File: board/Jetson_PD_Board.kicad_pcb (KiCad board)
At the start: 2 copper layers, 28 parts, among them J1 USB4081-03-A, J2 768250002, Q1 NTTFS5C673NLTAG, Q2 NTTFS5C673NLTAG, Q3 NTTFS5C673NLTAG, U1 APK43070DKZ-13-FA01, U2 USBLC6-2SC6

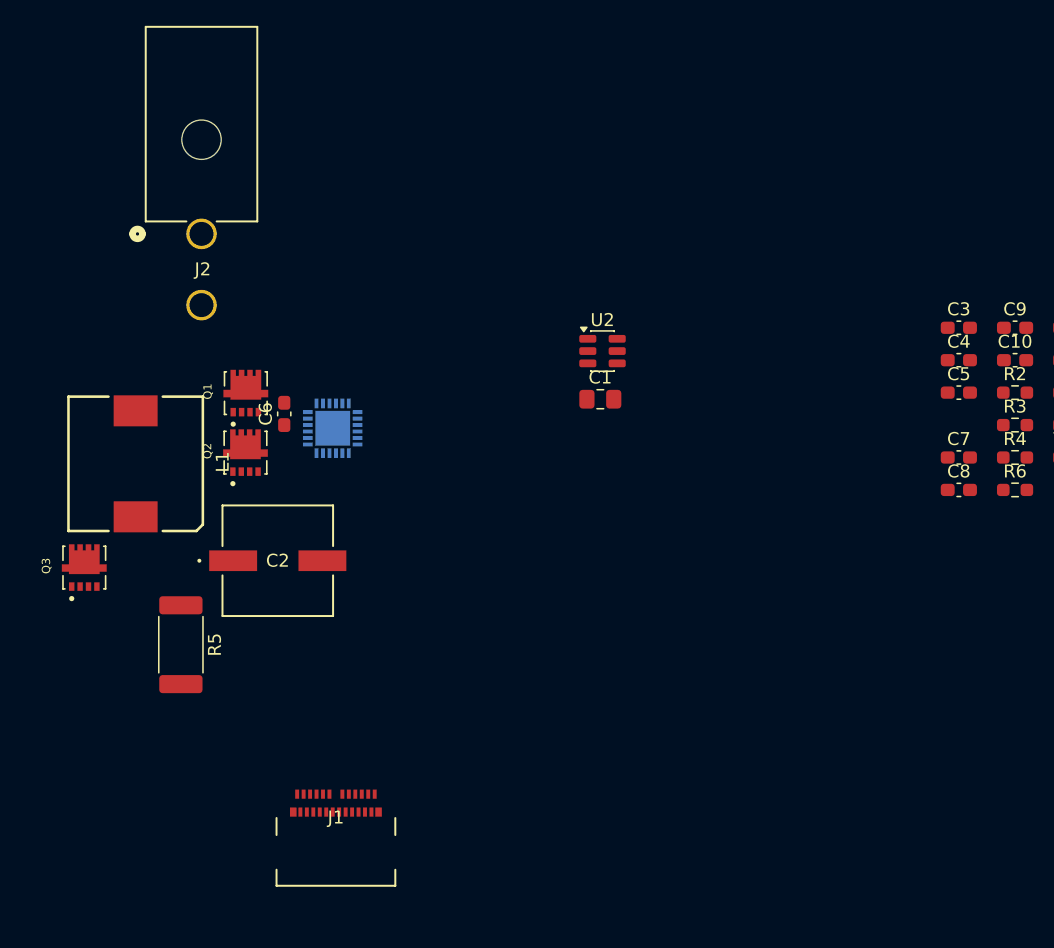
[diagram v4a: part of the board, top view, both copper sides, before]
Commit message: Labeled switching node
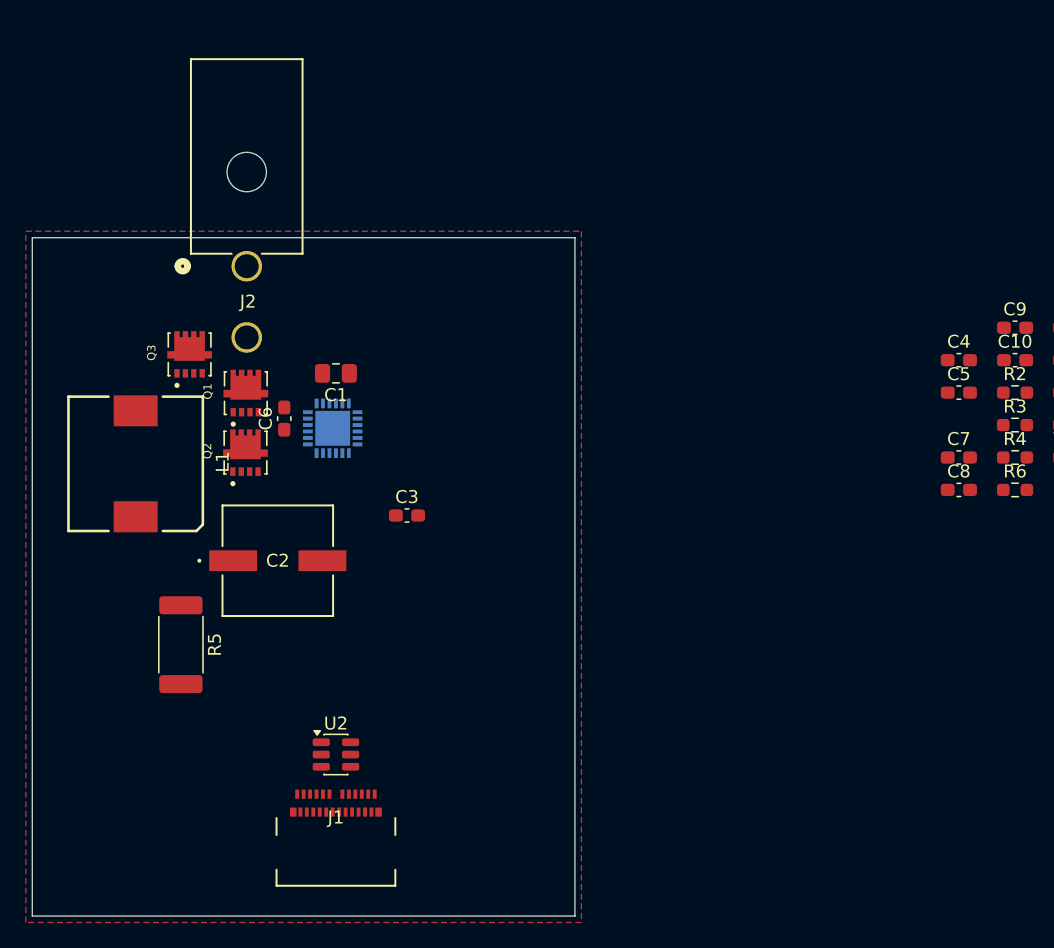
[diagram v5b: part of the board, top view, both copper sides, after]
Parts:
- moved C3 45.1 mm to (147.5, 105.5)
- moved U2 37.4 mm to (142.0, 124.0)
- moved C1 20.6 mm to (142.0, 94.5), turned to 180 degrees
- moved Q3 18.4 mm to (130.7, 93.0)
- moved J2 4.30 mm to (135.1, 86.2)
- moved C6 0.36 mm to (138.0, 98.0)
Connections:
- net Net-(Q1-S) renamed /Switching_Node
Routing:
- added copper zone on F.Cu, net GND
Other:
- board outline added: 42 x 52.5 mm
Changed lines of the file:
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@@
 	(net 6 "Net-(C5-Pad1)")
 	(net 7 "Net-(U1-VFB)")
-	(net 8 "Net-(Q1-S)")
+	(net 8 "/Switching_Node")
 	(net 9 "Net-(U1-BST)")
 	(net 10 "Net-(U1-V5V)")
@@
 			(size 2.4 3.4)
 			(layers "F.Cu" "F.Mask" "F.Paste")
-			(net 8 "Net-(Q1-S)")
+			(net 8 "/Switching_Node")
 			(pinfunction "1")
 			(pintype "passive")
@@
 	(footprint "PD_Hardware_Footprints:TRANS_NVTFS5116PLTAG"
 		(layer "F.Cu")
-		(at 122.525 109.53 90)
+		(at 130.675 93.03 90)
 		(property "Reference" "Q3"
 			(at 0.127 -2.9464 90)
@@
 			(size 0.66 0.42)
 			(layers "F.Cu" "F.Mask")
-			(net 8 "Net-(Q1-S)")
+			(net 8 "/Switching_Node")
 			(pinfunction "S")
 			(pintype "passive")
@@
 			(size 0.66 0.42)
 			(layers "F.Cu" "F.Mask")
-			(net 8 "Net-(Q1-S)")
+			(net 8 "/Switching_Node")
 			(pinfunction "S")
 			(pintype "passive")
@@
 			(size 0.66 0.42)
 			(layers "F.Cu" "F.Mask")
-			(net 8 "Net-(Q1-S)")
+			(net 8 "/Switching_Node")
 			(pinfunction "S")
 			(pintype "passive")
@@
 	(footprint "Package_TO_SOT_SMD:SOT-23-6"
 		(layer "F.Cu")
-		(at 162.6325 92.775)
+		(at 142 124)
 		(descr "SOT, 6 Pin (JEDEC MO-178 Var AB https://www.jedec.org/document_search?search_api_views_fulltext=MO-178), generated with kicad-footprint-generator ipc_gullwing_generator.py")
 		(tags "SOT TO_SOT_SMD")
@@
 	(footprint "PD_Hardware_Footprints:CONN_SD-76825-0100_02_MOL"
 		(layer "F.Cu")
-		(at 131.5969 83.70535 180)
+		(at 135.0969 86.20535 180)
 		(property "Reference" "J2"
 			(at -0.1016 -2.7432 0)
@@
 	(footprint "Capacitor_SMD:C_0805_2012Metric_Pad1.18x1.45mm_HandSolder"
 		(layer "F.Cu")
-		(at 162.4625 96.5)
+		(at 142 94.5 180)
 		(descr "Capacitor SMD 0805 (2012 Metric), square (rectangular) end terminal, IPC-7351 nominal with elongated pad for handsoldering. (Body size source: IPC-SM-782 page 76, https://www.pcb-3d.com/wordpress/wp-content/uploads/ipc-sm-782a_amendment_1_and_2.pdf, https://docs.google.com/spreadsheets/d/1BsfQQcO9C6DZCsRaXUlFlo91Tg2WpOkGARC1WS5S8t0/edit?usp=sharing), generated with kicad-footprint-generator")
 		(tags "capacitor handsolder")
@@
 		(attr smd)
 		(fp_line
-			(start -0.261252 -0.735)
-			(end 0.261252 -0.735)
+			(start -0.261252 0.735)
+			(end 0.261252 0.735)
 			(stroke
 				(width 0.12)
@@
 		)
 		(fp_line
-			(start -0.261252 0.735)
-			(end 0.261252 0.735)
+			(start -0.261252 -0.735)
+			(end 0.261252 -0.735)
 			(stroke
 				(width 0.12)
@@
 		)
 		(fp_line
-			(start -1.88 -0.98)
-			(end 1.88 -0.98)
+			(start 1.88 0.98)
+			(end -1.88 0.98)
 			(stroke
 				(width 0.05)
@@
 		)
 		(fp_line
-			(start -1.88 0.98)
-			(end -1.88 -0.98)
+			(start 1.88 -0.98)
+			(end 1.88 0.98)
 			(stroke
 				(width 0.05)
@@
 		)
 		(fp_line
-			(start 1.88 -0.98)
-			(end 1.88 0.98)
+			(start -1.88 0.98)
+			(end -1.88 -0.98)
 			(stroke
 				(width 0.05)
@@
 		)
 		(fp_line
-			(start 1.88 0.98)
-			(end -1.88 0.98)
+			(start -1.88 -0.98)
+			(end 1.88 -0.98)
 			(stroke
 				(width 0.05)
@@
 		)
 		(fp_line
-			(start -1 -0.625)
-			(end 1 -0.625)
+			(start 1 0.625)
+			(end -1 0.625)
 			(stroke
 				(width 0.1)
@@
 		)
 		(fp_line
-			(start -1 0.625)
-			(end -1 -0.625)
+			(start 1 -0.625)
+			(end 1 0.625)
 			(stroke
 				(width 0.1)
@@
 		)
 		(fp_line
-			(start 1 -0.625)
-			(end 1 0.625)
+			(start -1 0.625)
+			(end -1 -0.625)
 			(stroke
 				(width 0.1)
@@
 		)
 		(fp_line
-			(start 1 0.625)
-			(end -1 0.625)
+			(start -1 -0.625)
+			(end 1 -0.625)
 			(stroke
 				(width 0.1)
@@
 		)
 		(pad "1" smd roundrect
-			(at -1.0375 0)
+			(at -1.0375 0 180)
 			(size 1.175 1.45)
 			(layers "F.Cu" "F.Mask" "F.Paste")
@@
 		)
 		(pad "2" smd roundrect
-			(at 1.0375 0)
+			(at 1.0375 0 180)
 			(size 1.175 1.45)
 			(layers "F.Cu" "F.Mask" "F.Paste")
@@
 	(footprint "Capacitor_SMD:C_0603_1608Metric_Pad1.08x0.95mm_HandSolder"
 		(layer "F.Cu")
-		(at 190.2125 90.97)
+		(at 147.5 105.5)
 		(descr "Capacitor SMD 0603 (1608 Metric), square (rectangular) end terminal, IPC-7351 nominal with elongated pad for handsoldering. (Body size source: IPC-SM-782 page 76, https://www.pcb-3d.com/wordpress/wp-content/uploads/ipc-sm-782a_amendment_1_and_2.pdf), generated with kicad-footprint-generator")
 		(tags "capacitor handsolder")
@@
 	(footprint "Capacitor_SMD:C_0603_1608Metric_Pad1.08x0.95mm_HandSolder"
 		(layer "F.Cu")
-		(at 138 97.6375 90)
+		(at 138 98 90)
 		(descr "Capacitor SMD 0603 (1608 Metric), square (rectangular) end terminal, IPC-7351 nominal with elongated pad for handsoldering. (Body size source: IPC-SM-782 page 76, https://www.pcb-3d.com/wordpress/wp-content/uploads/ipc-sm-782a_amendment_1_and_2.pdf), generated with kicad-footprint-generator")
 		(tags "capacitor handsolder")
@@
 			(layers "F.Cu" "F.Mask" "F.Paste")
 			(roundrect_rratio 0.25)
-			(net 8 "Net-(Q1-S)")
+			(net 8 "/Switching_Node")
 			(pintype "passive")
 		)
@@
 			(size 0.635 1.27)
 			(layers "F.Cu")
-			(net 8 "Net-(Q1-S)")
+			(net 8 "/Switching_Node")
 			(pinfunction "D")
 			(pintype "passive")
@@
 			(size 0.75 0.3)
 			(layers "B.Cu" "B.Mask" "B.Paste")
-			(net 8 "Net-(Q1-S)")
+			(net 8 "/Switching_Node")
 			(pinfunction "SW")
 			(pintype "output")
@@
 			)
 		)
+	)
+	(gr_rect
+		(start 118.5 84)
+		(end 160.5 136.5)
+		(stroke
+			(width 0.05)
+			(type default)
+		)
+		(fill no)
+		(layer "Edge.Cuts")
+	)
+	(zone
+		(net 1)
+		(net_name "GND")
+		(layer "F.Cu")
+		(hatch edge 0.5)
+		(connect_pads
+			(clearance 0.5)
+		)
+		(min_thickness 0.25)
+		(filled_areas_thickness no)
+		(fill yes
+			(thermal_gap 0.5)
+			(thermal_bridge_width 0.5)
+		)
+		(polygon
+			(pts
+				(xy 118 83.5) (xy 161 83.5) (xy 161 137) (xy 118 137)
+			)
+		)

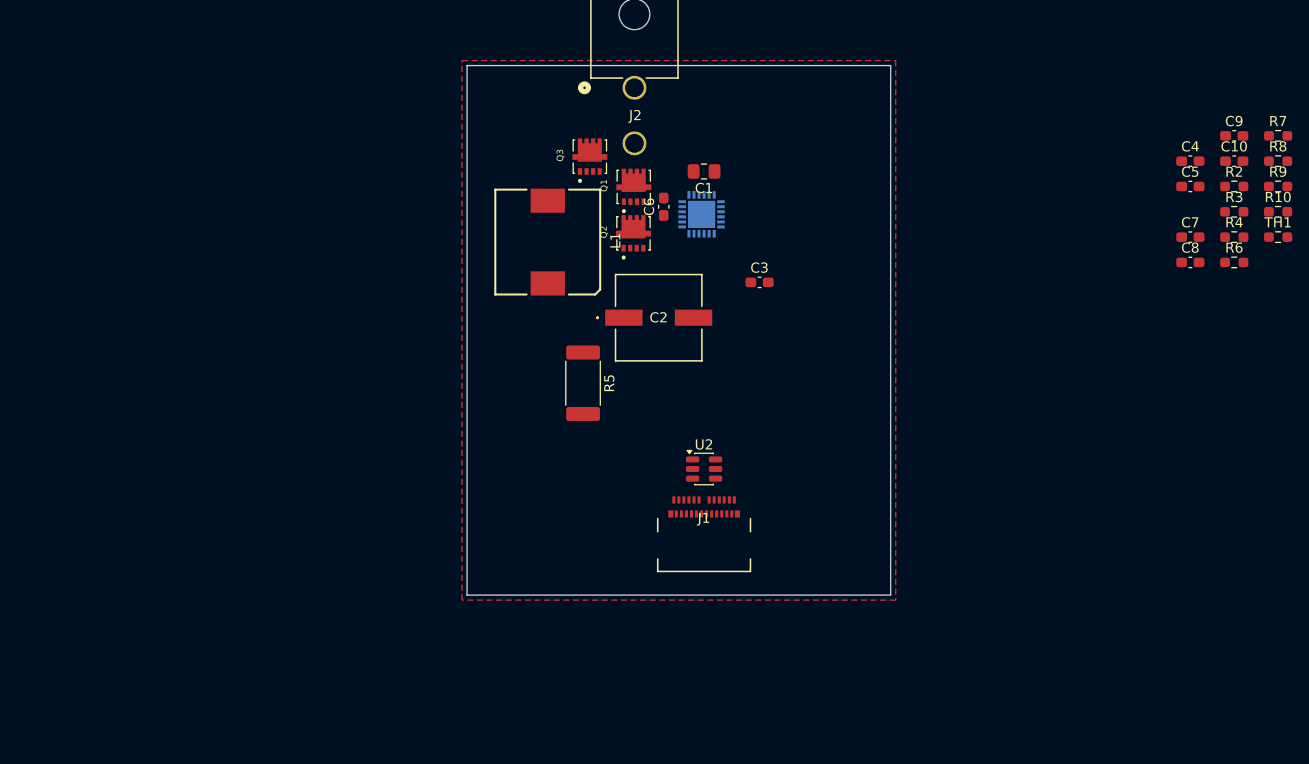
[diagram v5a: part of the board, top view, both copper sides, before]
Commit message: Added mounting holes, indicator LED, and cleaned up shcematic
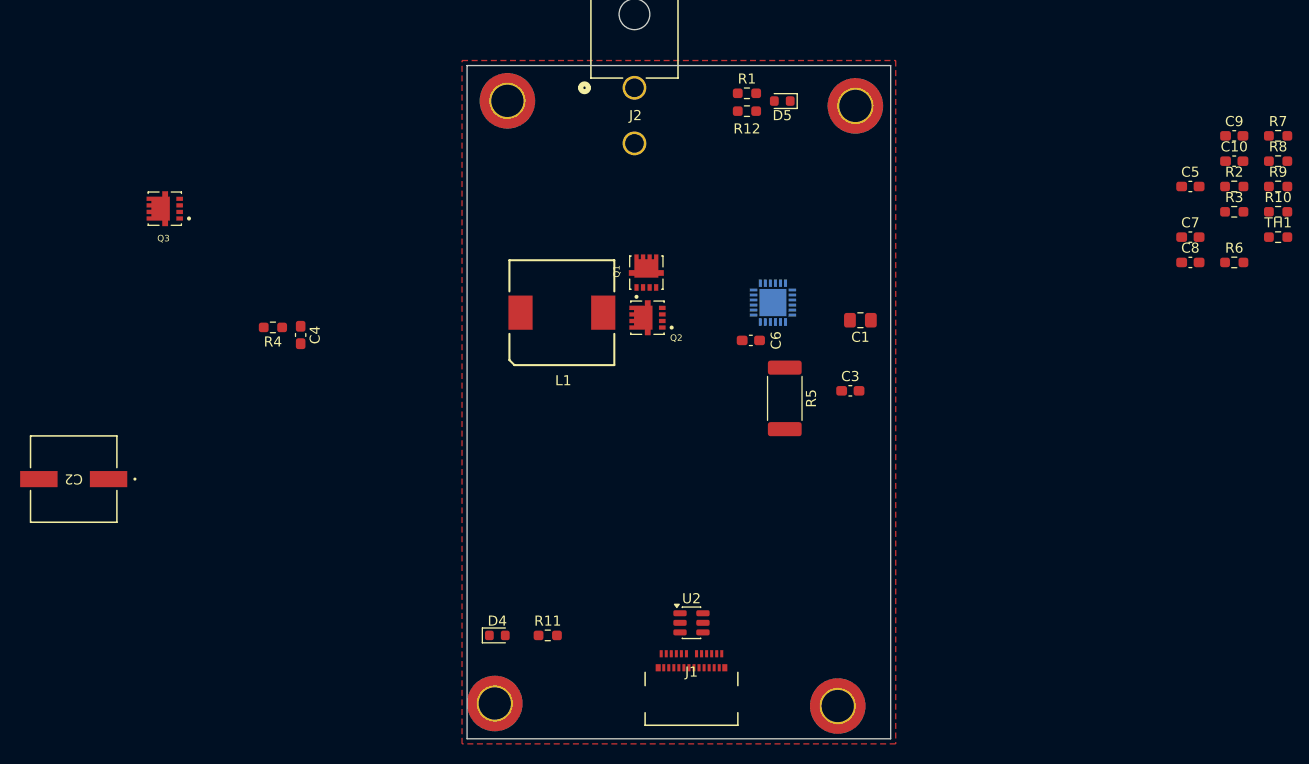
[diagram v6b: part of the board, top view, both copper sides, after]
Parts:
- added D4: LED (Blue), LED_SMD:LED_0603_1608Metric, F.Cu at (121.5, 140.5)
- added D5: LED (Yellow), LED_SMD:LED_0603_1608Metric, F.Cu at (149.8, 87.5)
- added H1: MountingHole, MountingHole:MountingHole_3.2mm_M3_ISO14580_Pad_TopBottom, F.Cu at (157.0, 88.0)
- added H2: MountingHole, MountingHole:MountingHole_3.2mm_M3_ISO14580_Pad_TopBottom, F.Cu at (121.2, 147.2)
- added H3: MountingHole, MountingHole:MountingHole_3.2mm_M3_ISO14580_Pad_TopBottom, F.Cu at (122.5, 87.5)
- added H4: MountingHole, MountingHole:MountingHole_3.2mm_M3_ISO14580_Pad_TopBottom, F.Cu at (155.2, 147.5)
- added R1: 2.2k, Resistor_SMD:R_0603_1608Metric_Pad0.98x0.95mm_HandSolder, F.Cu at (146.2, 86.8)
- added R11: 820, Resistor_SMD:R_0603_1608Metric_Pad0.98x0.95mm_HandSolder, F.Cu at (126.5, 140.5)
- added R12: 2.2k, Resistor_SMD:R_0603_1608Metric_Pad0.98x0.95mm_HandSolder, F.Cu at (146.2, 88.5)
- moved R4 95.7 mm to (99.2, 110.0), turned to 180 degrees
- moved C4 89.9 mm to (102.0, 110.7), turned to -90 degrees
- moved C2 60.2 mm to (79.5, 125.0), turned to 180 degrees
- moved Q3 42.5 mm to (88.5, 98.2), turned to 180 degrees
- moved C1 21.4 mm to (157.5, 109.2)
- moved R5 20.1 mm to (150.0, 117.0)
- moved C6 15.8 mm to (146.6, 111.2), turned to 0 degrees
- moved J1 15.3 mm to (140.8, 145.8)
- moved U2 15.3 mm to (140.8, 139.2)
- moved C3 14.0 mm to (156.5, 116.2)
- moved U1 11.3 mm to (148.8, 107.5)
- moved Q1 8.59 mm to (136.3, 104.5)
- moved Q2 8.48 mm to (136.4, 109.0), turned to 180 degrees
- moved L1 7.14 mm to (127.9, 108.5), turned to 180 degrees
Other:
- board size 42 x 52.5 mm -> 42 x 66.8 mm

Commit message: Updated schematic in accordance with design guide
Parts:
- added C11: 1nF, Capacitor_SMD:C_0603_1608Metric_Pad1.08x0.95mm_HandSolder, F.Cu at (230.7, 100.3)
- added C12: 10uF, Capacitor_SMD:C_1206_3216Metric_Pad1.33x1.80mm_HandSolder, F.Cu at (216.2, 128.1)
- added C13: 10uF, Capacitor_SMD:C_1206_3216Metric_Pad1.33x1.80mm_HandSolder, F.Cu at (216.2, 131.5)
- added C14: 0.1uF, Capacitor_SMD:C_0603_1608Metric_Pad1.08x0.95mm_HandSolder, F.Cu at (230.7, 102.8)
- added D1: 1N4148WS, Diode_SMD:D_SOD-323, F.Cu at (221.4, 133.1)
- added R13: 33k, Resistor_SMD:R_0603_1608Metric_Pad0.98x0.95mm_HandSolder, F.Cu at (239.4, 97.8)
- added R14: 22, Resistor_SMD:R_0603_1608Metric_Pad0.98x0.95mm_HandSolder, F.Cu at (239.4, 100.3)
- added R15: 22, Resistor_SMD:R_0603_1608Metric_Pad0.98x0.95mm_HandSolder, F.Cu at (239.4, 102.8)
- added R16: 22, Resistor_SMD:R_0603_1608Metric_Pad0.98x0.95mm_HandSolder, F.Cu at (239.4, 105.3)
- added R17: 22, Resistor_SMD:R_0603_1608Metric_Pad0.98x0.95mm_HandSolder, F.Cu at (239.4, 107.8)
- C7, C8: value 15uF -> 1uF
- L1: value L -> 13uH
- R6, R7: value 100k -> 4.7k
- U1: moved to F.Cu
- moved H2 185.8 mm to (270.8, 37.0)
- moved Q3 156.5 mm to (244.7, 109.0), turned to 0 degrees
- moved H3 154.5 mm to (270.8, 44.0)
- moved C2 151.5 mm to (230.9, 119.3), turned to 0 degrees
- moved H4 150.5 mm to (270.8, 51.0)
- moved R4 131.5 mm to (230.7, 112.8), turned to 0 degrees
- moved H1 127.7 mm to (270.8, 29.9)
- moved C4 124.8 mm to (226.4, 100.3), turned to 0 degrees
- moved R11 112.7 mm to (235.1, 110.3)
- moved Q1 108.6 mm to (244.7, 99.0), turned to 0 degrees
- moved Q2 108.4 mm to (244.7, 104.0), turned to 0 degrees
- moved L1 104.7 mm to (230.2, 130.5), turned to 0 degrees
- moved J1 103.1 mm to (242.7, 130.5)
- moved U2 100.7 mm to (239.9, 121.4)
- moved D4 100.6 mm to (221.3, 127.7)
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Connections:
- C1 pad 1: V_{out} -> Net-(D1-A)
- C2 pad 1: Net-(Q3-S) -> Net-(D1-A)
- C8 pad 1: GND -> Net-(U1-VDRV)
- C8 pad 2: Net-(U1-VDRV) -> GND
- L1 pad 2: Net-(Q3-S) -> Net-(D1-A)
- Q3 pad 2: Net-(Q3-G) -> Net-(D1-K)
- Q3 pad 3: Net-(Q3-S) -> Net-(D1-A)
- R5 pad 1: Net-(Q3-S) -> Net-(D1-A)
- U1 pad 19: Net-(Q3-G) -> Net-(U1-GATE)
- U1 pad 2: CC1 -> Net-(U1-CC1)
- U1 pad 24: Net-(Q3-S) -> Net-(D1-A)
- U1 pad 3: CC2 -> Net-(U1-CC2)
- U2 pad 1: Net-(U1-DP) -> Net-(R14-Pad2)
- U2 pad 3: Net-(U1-DN) -> Net-(R15-Pad2)
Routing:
- removed copper zone on F.Cu, net GND
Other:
- board outline removed

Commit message: Switch-node placement
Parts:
- moved Q3 129.4 mm to (117.4, 85.7), turned to 90 degrees
- moved Q2 120.0 mm to (125.0, 95.7), turned to 180 degrees
- moved Q1 119.9 mm to (125.0, 91.0), turned to 90 degrees
- moved L1 118.9 mm to (117.1, 93.9), turned to 180 degrees
- moved J1 115.3 mm to (127.5, 125.5)
- moved U1 89.8 mm to (135.6, 86.0), turned to -135 degrees
- moved J2 83.8 mm to (123.4, 80.3), turned to 180 degrees
- moved C1 67.1 mm to (183.3, 93.8)
- moved D1 67.1 mm to (159.9, 106.4)
- moved D4 67.1 mm to (159.8, 101.1)
- moved D5 67.1 mm to (159.8, 103.7)
- moved R13 67.1 mm to (177.9, 71.1)
- moved R14 67.1 mm to (177.9, 73.6)
- moved R15 67.1 mm to (177.9, 76.1)
- moved R16 67.1 mm to (177.9, 78.6)
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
